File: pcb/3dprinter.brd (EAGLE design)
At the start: 100 x 80 mm, 16 parts, among them IC1 TMC2100

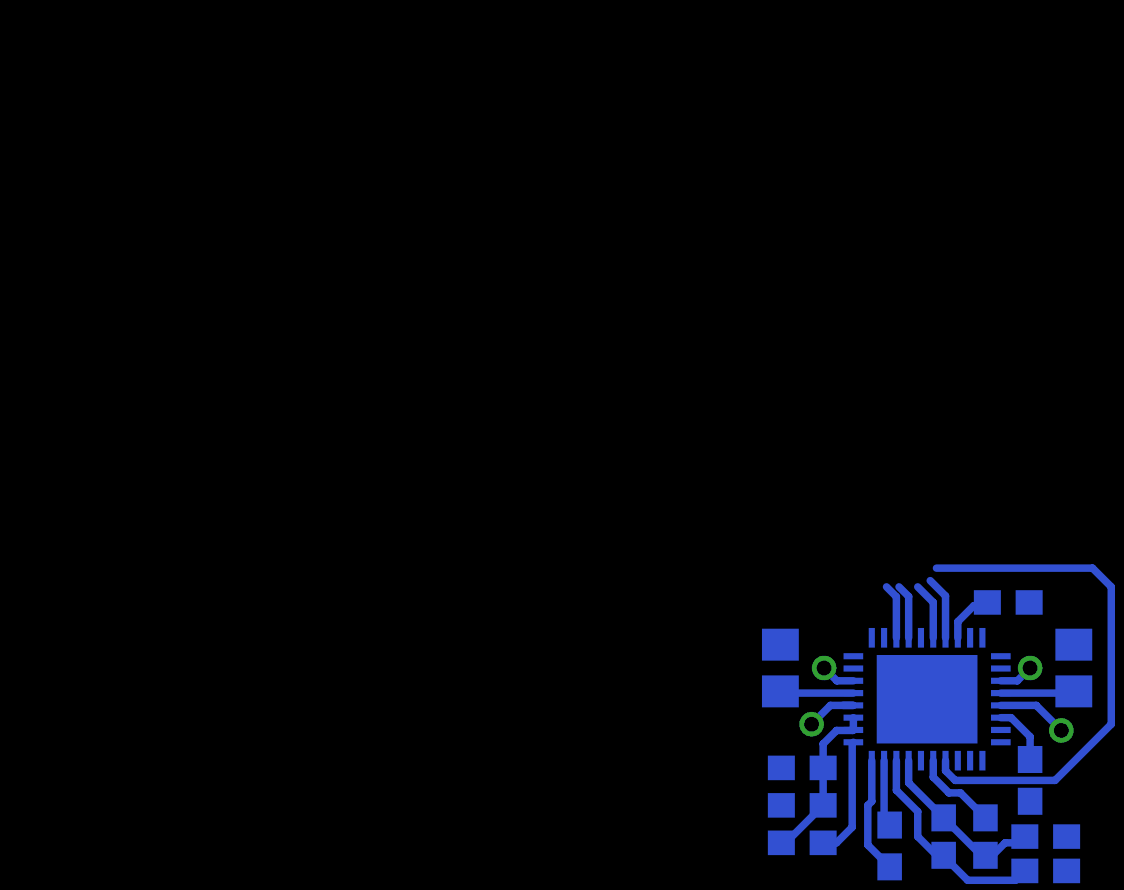
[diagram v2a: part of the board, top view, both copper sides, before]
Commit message: Added NRF51822 footprint
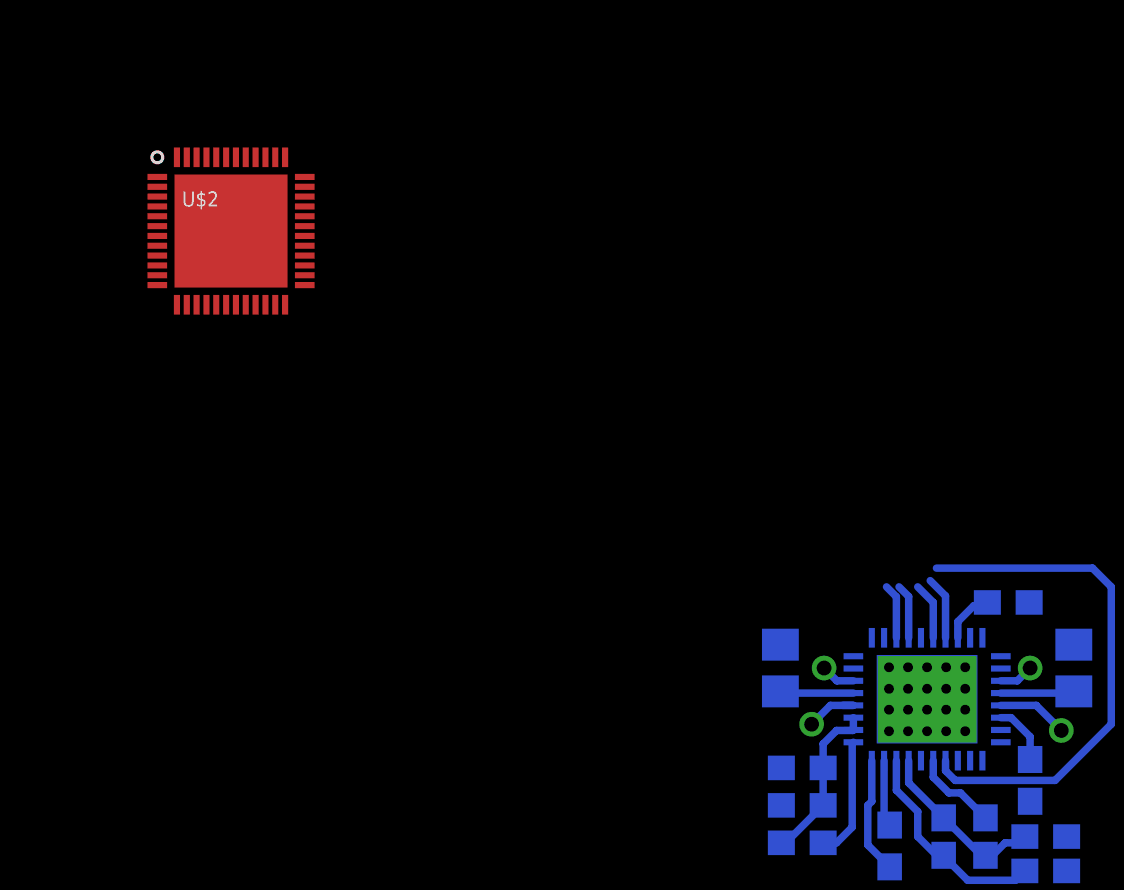
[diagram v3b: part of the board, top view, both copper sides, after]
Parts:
- added U$2: NRF51822, 3dprinter:QFN48
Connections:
- new net PI_02_SDA1: PI_HEADER.3
- new net PI_03_SCL1: PI_HEADER.5
- new net PI_04: PI_HEADER.7
- new net PI_05: PI_HEADER.29
- new net PI_06: PI_HEADER.31
- new net PI_07_CE1: PI_HEADER.26
- new net PI_08_CE0: PI_HEADER.24
- new net PI_09_MISO: PI_HEADER.21
- new net PI_10_MOSI: PI_HEADER.19
- new net PI_11_SCK: PI_HEADER.23
- new net PI_12: PI_HEADER.32
- new net PI_13: PI_HEADER.33
- new net PI_14_TXD0: PI_HEADER.8
- new net PI_15_RXD0: PI_HEADER.10
- new net PI_16: PI_HEADER.36
- new net PI_17: PI_HEADER.11
- new net PI_18: PI_HEADER.12
- new net PI_19: PI_HEADER.35
- new net PI_20: PI_HEADER.38
- new net PI_21: PI_HEADER.40
- new net PI_22: PI_HEADER.15
- new net PI_23: PI_HEADER.16
- new net PI_24: PI_HEADER.18
- new net PI_25: PI_HEADER.22
- new net PI_26: PI_HEADER.37
- new net PI_27: PI_HEADER.13
- new net PI_3V32: PI_HEADER.17
- new net PI_5V1: PI_HEADER.2
- new net PI_5V2: PI_HEADER.4
- new net PI_GND1: PI_HEADER.9
- new net PI_GND2: PI_HEADER.25
- new net PI_GND3: PI_HEADER.39
- new net PI_GND4: PI_HEADER.6
- new net PI_GND5: PI_HEADER.14
- new net PI_GND6: PI_HEADER.20
- new net PI_GND7: PI_HEADER.30
- new net PI_GND8: PI_HEADER.34
- new net PI_ID_SC: PI_HEADER.28
- new net PI_ID_SD: PI_HEADER.27
- net GND: now also IC1.TVIA1, IC1.TVIA10, IC1.TVIA11, IC1.TVIA12, IC1.TVIA13, IC1.TVIA14, IC1.TVIA15, IC1.TVIA16, IC1.TVIA17, IC1.TVIA18, IC1.TVIA19, IC1.TVIA2, IC1.TVIA20, IC1.TVIA3, IC1.TVIA4, IC1.TVIA5, IC1.TVIA6, IC1.TVIA7, IC1.TVIA8, IC1.TVIA9
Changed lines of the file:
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@@
 <attribute name="OC_NEWARK" value="unknown" x="51.943" y="2.921" size="1.778" layer="27" display="off"/>
 </element>
+<element name="U$2" library="3dprinter" package="QFN48" value="NRF51822" x="28.194" y="34.036"/>
 </elements>
 <signals>
@@
 </signal>
 <signal name="PI_02_SDA1">
+<contactref element="PI_HEADER" pad="3"/>
 </signal>
 <signal name="PI_03_SCL1">
+<contactref element="PI_HEADER" pad="5"/>
 </signal>
 <signal name="PI_04">
+<contactref element="PI_HEADER" pad="7"/>
 </signal>
 <signal name="PI_GND1">
+<contactref element="PI_HEADER" pad="9"/>
 </signal>
 <signal name="PI_17">
+<contactref element="PI_HEADER" pad="11"/>
 </signal>
 <signal name="PI_27">
+<contactref element="PI_HEADER" pad="13"/>
 </signal>
 <signal name="PI_22">
+<contactref element="PI_HEADER" pad="15"/>
 </signal>
 <signal name="PI_3V32">
+<contactref element="PI_HEADER" pad="17"/>
 </signal>
 <signal name="PI_09_MISO">
+<contactref element="PI_HEADER" pad="21"/>
 </signal>
 <signal name="PI_11_SCK">
+<contactref element="PI_HEADER" pad="23"/>
 </signal>
 <signal name="PI_GND2">
+<contactref element="PI_HEADER" pad="25"/>
 </signal>
 <signal name="PI_ID_SD">
+<contactref element="PI_HEADER" pad="27"/>
 </signal>
 <signal name="PI_05">
+<contactref element="PI_HEADER" pad="29"/>
 </signal>
 <signal name="PI_06">
+<contactref element="PI_HEADER" pad="31"/>
 </signal>
 <signal name="PI_13">
+<contactref element="PI_HEADER" pad="33"/>
 </signal>
 <signal name="PI_19">
+<contactref element="PI_HEADER" pad="35"/>
 </signal>
 <signal name="PI_26">
+<contactref element="PI_HEADER" pad="37"/>
 </signal>
 <signal name="PI_5V1">
+<contactref element="PI_HEADER" pad="2"/>
 </signal>
 <signal name="PI_5V2">
+<contactref element="PI_HEADER" pad="4"/>
 </signal>
 <signal name="PI_GND4">
+<contactref element="PI_HEADER" pad="6"/>
 </signal>
 <signal name="PI_14_TXD0">
+<contactref element="PI_HEADER" pad="8"/>
 </signal>
 <signal name="PI_15_RXD0">
+<contactref element="PI_HEADER" pad="10"/>
 </signal>
 <signal name="PI_18">
+<contactref element="PI_HEADER" pad="12"/>
 </signal>
 <signal name="PI_GND5">
+<contactref element="PI_HEADER" pad="14"/>
 </signal>
 <signal name="PI_23">
+<contactref element="PI_HEADER" pad="16"/>
 </signal>
 <signal name="PI_24">
+<contactref element="PI_HEADER" pad="18"/>
 </signal>
 <signal name="PI_25">
+<contactref element="PI_HEADER" pad="22"/>
 </signal>
 <signal name="PI_08_CE0">
+<contactref element="PI_HEADER" pad="24"/>
 </signal>
 <signal name="PI_ID_SC">
+<contactref element="PI_HEADER" pad="28"/>
 </signal>
 <signal name="PI_GND7">
+<contactref element="PI_HEADER" pad="30"/>
 </signal>
 <signal name="PI_12">
+<contactref element="PI_HEADER" pad="32"/>
 </signal>
 <signal name="PI_GND8">
+<contactref element="PI_HEADER" pad="34"/>
 </signal>
 <signal name="PI_16">
+<contactref element="PI_HEADER" pad="36"/>
 </signal>
 <signal name="PI_20">
+<contactref element="PI_HEADER" pad="38"/>
 </signal>
 <signal name="+12V">
@@
 <wire x1="50.585" y1="12.192" x2="53.515" y2="16.236" width="0" layer="19" extent="16-16"/>
 <wire x1="50.585" y1="10.668" x2="50.585" y2="12.192" width="0" layer="19" extent="16-16"/>
+<contactref element="IC1" pad="TVIA1"/>
+<contactref element="IC1" pad="TVIA2"/>
+<contactref element="IC1" pad="TVIA3"/>
+<contactref element="IC1" pad="TVIA4"/>
+<contactref element="IC1" pad="TVIA5"/>
+<contactref element="IC1" pad="TVIA6"/>
+<contactref element="IC1" pad="TVIA7"/>
+<contactref element="IC1" pad="TVIA8"/>
+<contactref element="IC1" pad="TVIA9"/>
+<contactref element="IC1" pad="TVIA10"/>
+<contactref element="IC1" pad="TVIA11"/>
+<contactref element="IC1" pad="TVIA12"/>
+<contactref element="IC1" pad="TVIA13"/>
+<contactref element="IC1" pad="TVIA14"/>
+<contactref element="IC1" pad="TVIA15"/>
+<contactref element="IC1" pad="TVIA16"/>
+<contactref element="IC1" pad="TVIA17"/>
+<contactref element="IC1" pad="TVIA18"/>
+<contactref element="IC1" pad="TVIA19"/>
+<contactref element="IC1" pad="TVIA20"/>
 </signal>
 <signal name="CPI_M1">
@@
 <wire x1="56.134" y1="10.414" x2="55.265" y2="11.283" width="0.3048" layer="16"/>
 </signal>
+<signal name="PI_GND3">
+<contactref element="PI_HEADER" pad="39"/>
+</signal>
+<signal name="PI_10_MOSI">
+<contactref element="PI_HEADER" pad="19"/>
+</signal>
+<signal name="PI_GND6">
+<contactref element="PI_HEADER" pad="20"/>
+</signal>
+<signal name="PI_07_CE1">
+<contactref element="PI_HEADER" pad="26"/>
+</signal>
+<signal name="PI_21">
+<contactref element="PI_HEADER" pad="40"/>
+</signal>
 </signals>

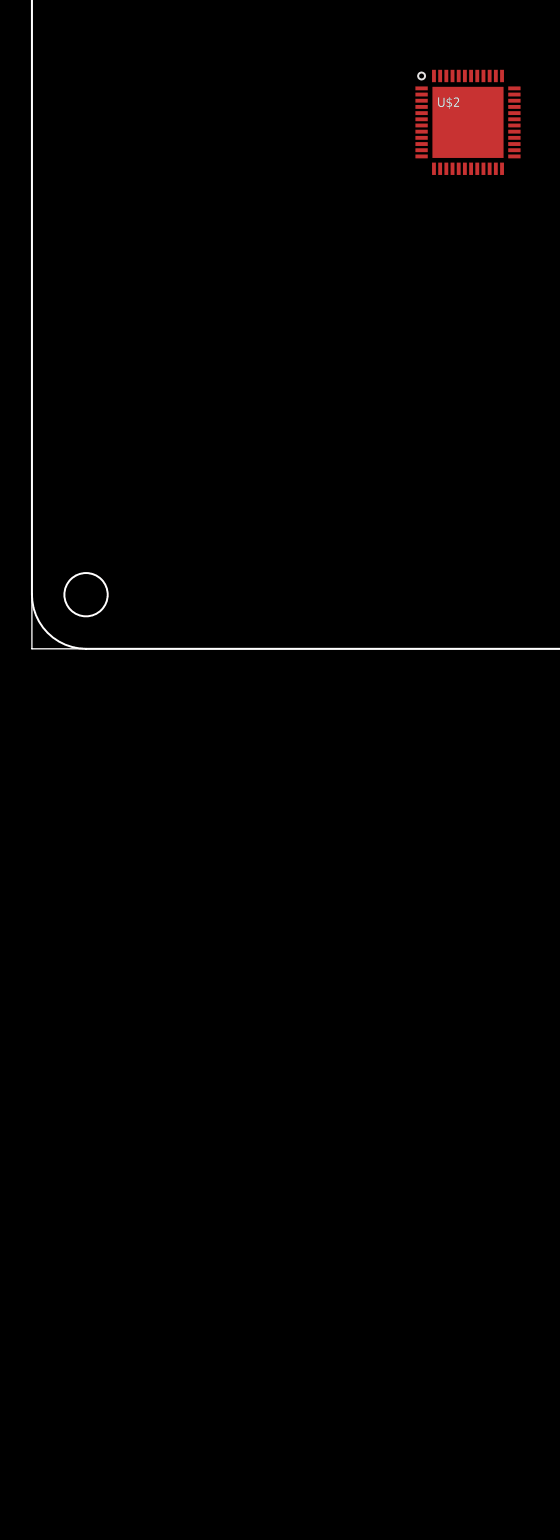
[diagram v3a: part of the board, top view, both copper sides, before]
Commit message: Example circuit nrf51 passives
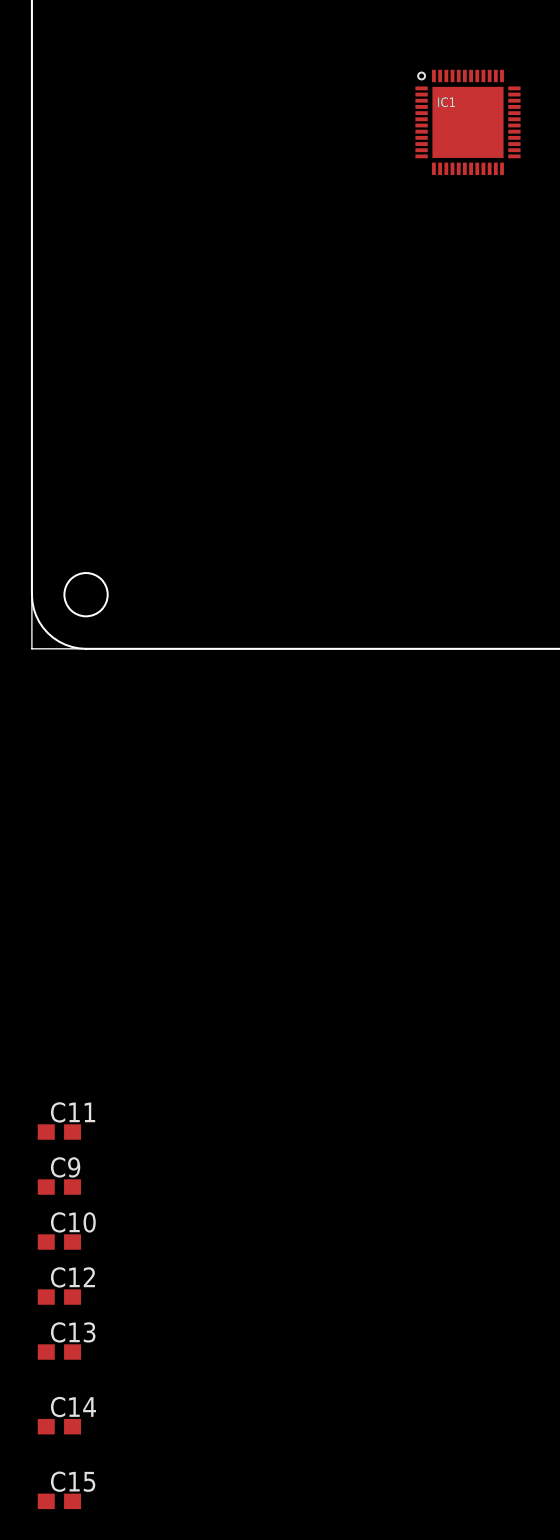
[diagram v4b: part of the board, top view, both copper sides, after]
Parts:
- removed U$2: NRF51822, 3dprinter:QFN48
- added C10: 47n, 3dprinter:C0603
- added C11, C9: 12p, 3dprinter:C0603
- added C12, C13, C14: 100n, 3dprinter:C0603
- added C15: 1n, 3dprinter:C0603
- added IC2: TMC2100, 3dprinter:QFN36
- IC1: value TMC2100 -> NRF51822; device 3dprinter:QFN36 -> 3dprinter:QFN48
- moved IC1 34.1 mm to (28.2, 34.0), flipped to the top, turned to 0 degrees
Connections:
- removed net PI_3V31: PI_HEADER.1
- removed net PI_3V32: PI_HEADER.17
- removed net PI_5V1: PI_HEADER.2
- removed net PI_5V2: PI_HEADER.4
- removed net PI_GND1: PI_HEADER.9
- removed net PI_GND2: PI_HEADER.25
- removed net PI_GND3: PI_HEADER.39
- removed net PI_GND4: PI_HEADER.6
- removed net PI_GND5: PI_HEADER.14
- removed net PI_GND6: PI_HEADER.20
- removed net PI_GND7: PI_HEADER.30
- removed net PI_GND8: PI_HEADER.34
- new net +3V3: PI_HEADER.1, PI_HEADER.17
- new net N$1: C9.1, IC1.38
- new net N$2: C11.1, IC1.37
- new net N$3: C12.1, IC1.39
- new net N$4: C10.1, IC1.29
- new net N$5: C13.1, C14.1, IC1.1, IC1.12
- new net N$6: C15.1, IC1.35, IC1.36
- net +12V: now also IC2.16, IC2.30, IC2.31; no longer IC1.16, IC1.30, IC1.31
- net +5V: now also IC2.8, PI_HEADER.2, PI_HEADER.4; no longer IC1.8
- net 5V_M1: now also IC2.25; no longer IC1.25
- net BRA_M1: now also IC2.33; no longer IC1.33
- net BRB_M1: now also IC2.14; no longer IC1.14
- net CFG1_M1: now also IC2.4; no longer IC1.4
- net CFG2_M1: now also IC2.3; no longer IC1.3
- net CPI_M1: now also IC2.28; no longer IC1.28
- net CPO_M1: now also IC2.27; no longer IC1.27
- net DIR_M1: now also IC2.7; no longer IC1.7
- net EN_M1: now also IC2.22; no longer IC1.22
- net GND: now also C10.2, C11.2, C12.2, C13.2, C14.2, C15.2, C9.2, IC1.13, IC1.33, IC1.34, IC2.1, IC2.10, IC2.11, IC2.12, IC2.24, IC2.35, IC2.36, IC2.5, IC2.PAD, IC2.TVIA1, IC2.TVIA10, IC2.TVIA11, IC2.TVIA12, IC2.TVIA13, IC2.TVIA14, IC2.TVIA15, IC2.TVIA16, IC2.TVIA17, IC2.TVIA18, IC2.TVIA19, IC2.TVIA2, IC2.TVIA20, IC2.TVIA3, IC2.TVIA4, IC2.TVIA5, IC2.TVIA6, IC2.TVIA7, IC2.TVIA8, IC2.TVIA9, PI_HEADER.14, PI_HEADER.20, PI_HEADER.25, PI_HEADER.30, PI_HEADER.34, PI_HEADER.39, PI_HEADER.6, PI_HEADER.9; no longer IC1.1, IC1.10, IC1.11, IC1.12, IC1.24, IC1.35, IC1.36, IC1.5, IC1.TVIA1, IC1.TVIA10, IC1.TVIA11, IC1.TVIA12, IC1.TVIA13, IC1.TVIA14, IC1.TVIA15, IC1.TVIA16, IC1.TVIA17, IC1.TVIA18, IC1.TVIA19, IC1.TVIA2, IC1.TVIA20, IC1.TVIA3, IC1.TVIA4, IC1.TVIA5, IC1.TVIA6, IC1.TVIA7, IC1.TVIA8, IC1.TVIA9
- net IREF_M1: now also IC2.23; no longer IC1.23
- net OA1_M1: now also IC2.34; no longer IC1.34
- net OA2_M1: now also IC2.32; no longer IC1.32
- net OB1_M1: now also IC2.13; no longer IC1.13
- net OB2_M1: now also IC2.15; no longer IC1.15
- net STEP_M1: now also IC2.6; no longer IC1.6
- net VCC_M1: now also IC2.26; no longer IC1.26
- net VCP_M1: now also IC2.29; no longer IC1.29
